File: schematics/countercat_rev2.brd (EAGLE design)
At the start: 50.8 x 50.8 mm, 30 parts, among them Q3 IRF520, Q4 IRF520, U4 ATMEGA328P_PDIP, Y1 16MHz

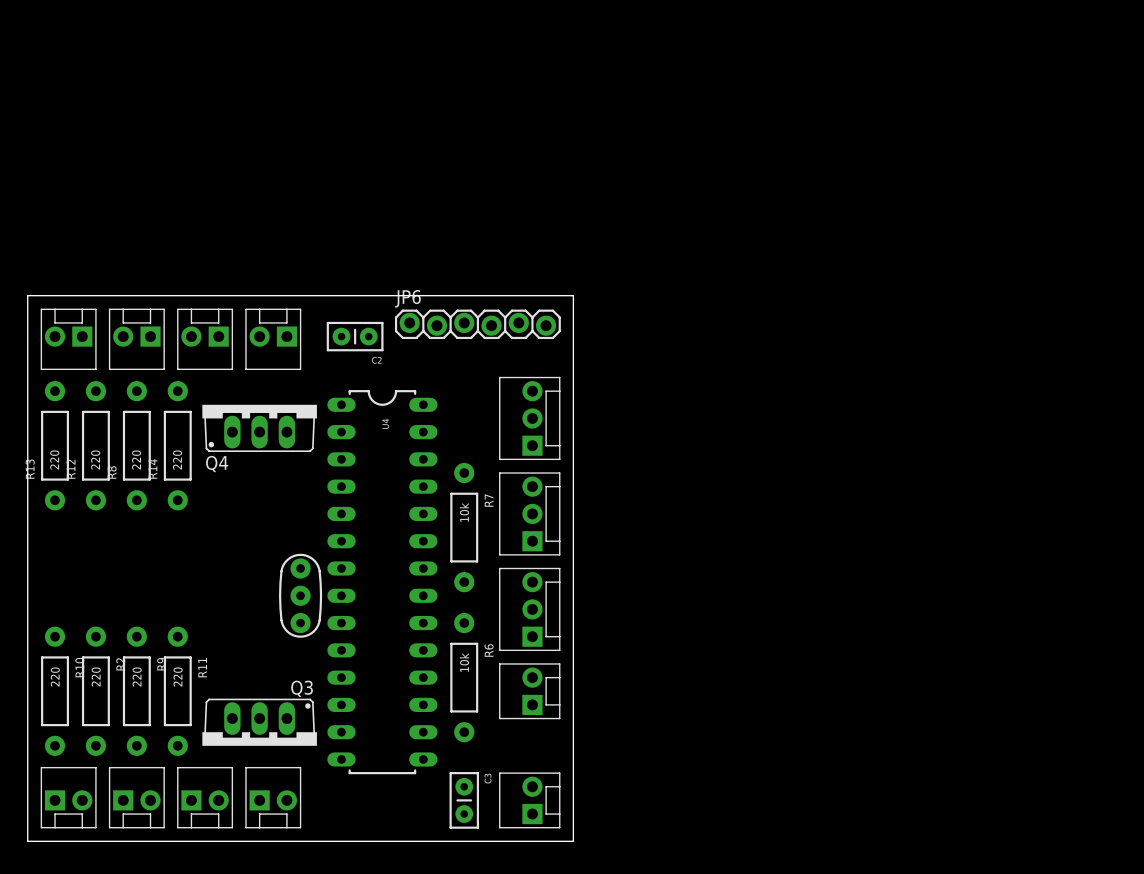
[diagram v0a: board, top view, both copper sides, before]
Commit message: Changed board size, add shifter
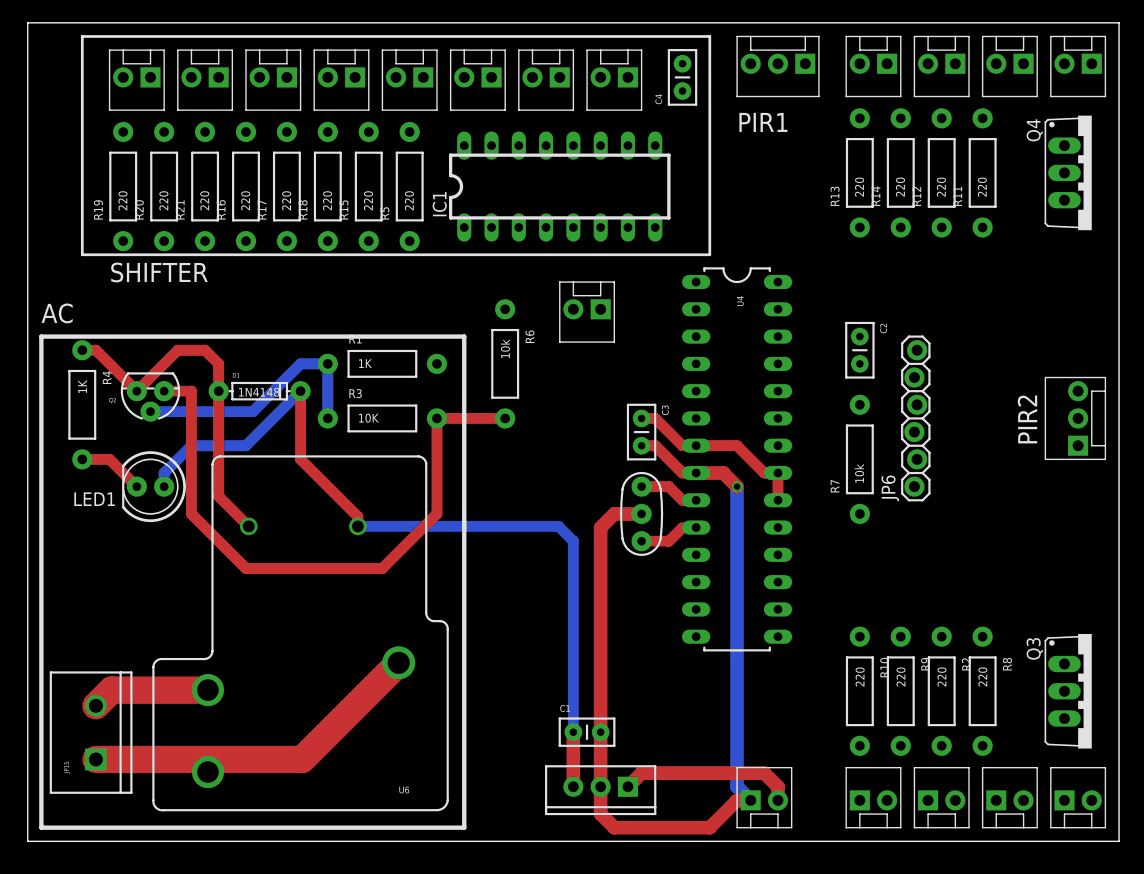
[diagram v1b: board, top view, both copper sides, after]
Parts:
- removed JP10: PWR, SparkFun:MOLEX-1X2
- added C1, C4: .1uF, SparkFun-Capacitors:CAP-PTH-SMALL2
- added D1: 1N4148, SparkFun:DIODE-1N4148
- added IC1: 74LS595N, SparkFun-DigitalIC:DIL16
- added JP15: Load, SparkFun:SCREWTERMINAL-5MM-2
- added JP16, JP17, JP18, JP19, JP20, JP21, JP22: RED1, SparkFun:MOLEX-1X2
- added JP23: PWR, SparkFun:MOLEX-1X2
- added LED1: (no value), SparkFun:LED5MM
- added LM7805: 5v, SparkFun-PowerIC:TO220-IGO
- added Q2: 2N3904, SparkFun:TO-92
- added R1, R4: 1K, SparkFun-Resistors:AXIAL-0.4
- added R15, R16, R17, R18, R19, R20, R21, R5: 220, SparkFun-Resistors:AXIAL-0.4
- added R3: 10K, SparkFun-Resistors:AXIAL-0.4
- added U6: RELAYPTH3, SparkFun:RELAY-T9A-2
- JP2: value RELAY -> RED1; device SparkFun:MOLEX-1X3 -> SparkFun:MOLEX-1X2
- moved JP11 108.3 mm to (99.1, 72.4), turned to 180 degrees
- moved R11 89.1 mm to (88.9, 62.2), turned to 90 degrees
- moved JP4 84.3 mm to (96.5, 3.81), turned to 0 degrees
- moved R12 82.7 mm to (85.1, 62.2)
- moved R8 82.0 mm to (88.9, 14.0), turned to 270 degrees
- moved JP3 81.3 mm to (90.2, 3.81)
- moved Q4 80.4 mm to (99.1, 62.2), turned to 270 degrees
- moved JP12 79.1 mm to (92.7, 72.4)
- moved JP13 79.1 mm to (80.0, 72.4)
- moved JP14 79.1 mm to (86.4, 72.4)
- moved R13 79.1 mm to (77.5, 62.2)
- moved R2 78.7 mm to (85.1, 14.0)
- moved Q3 77.6 mm to (99.1, 14.0), turned to 270 degrees
- moved JP8 74.9 mm to (77.5, 3.81)
- moved R10 74.9 mm to (77.5, 14.0)
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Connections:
- removed net FLASH: U4.15
- removed net N$12: C3.1
- removed net SPI_MISO: U4.18
- removed net SPI_MOSI: U4.17
- removed net SPI_SCK: U4.19
- new net COIL: D1.A, Q2.3, R4.P$1, U6.COIL2
- new net LOAD1: JP15.1, U6.MAIN
- new net LOAD2: JP15.2, U6.NO
- new net N$1: IC1.9
- new net N$10: JP2.1, R5.P$2
- new net N$11: JP16.1, R15.P$2
- new net N$14: JP19.1, R16.P$2
- new net N$17: JP18.1, R17.P$2
- new net N$20: JP17.1, R18.P$2
- new net N$23: JP22.1, R19.P$2
- new net N$24: JP21.1, R20.P$2
- new net N$25: JP20.1, R21.P$2
- new net N$26: IC1.15, R5.P$1
- new net N$27: IC1.1, R15.P$1
- new net N$28: IC1.2, R16.P$1
- new net N$29: IC1.3, R17.P$1
- new net N$30: IC1.4, R18.P$1
- new net N$31: IC1.5, R19.P$1
- new net N$32: IC1.6, R20.P$1
- new net N$33: IC1.7, R21.P$1
- new net N$6: Q2.2, R1.P$1, R3.P$1
- new net N$9: LED1.K, R4.P$2
- new net RCLK: IC1.12, U4.12
- new net SER: IC1.14, U4.6
- new net SRCLK: IC1.11, U4.11
- new net VB: JP23.2, LM7805.IN
- net 5V: now also C1.1, C4.2, D1.C, IC1.10, IC1.16, LED1.A, LM7805.OUT, U6.COIL1; no longer JP10.2, JP2.1
- net GND: now also C1.2, C4.1, IC1.13, IC1.8, JP16.2, JP17.2, JP18.2, JP19.2, JP20.2, JP21.2, JP22.2, JP23.1, LM7805.GND, Q2.1, R3.P$2; no longer JP10.1
- net N$8: now also C3.1
- net RELAY: now also R1.P$2; no longer JP2.3
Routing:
- net GND: track 0.00 -> 143.0 mm, vias 0 -> 1
- net 5V: track 0.00 -> 75.4 mm
- net COIL: track 0.00 -> 32.7 mm
- net LOAD1: track 0.00 -> 31.9 mm
- net N$6: track 0.00 -> 23.4 mm
- net N$8: track 0.00 -> 17.3 mm
- net VB: track 0.00 -> 16.3 mm
- net LOAD2: track 0.00 -> 11.0 mm
- net N$9: track 0.00 -> 6.13 mm
- net N$3: track 0.00 -> 5.61 mm
- net N$7: track 0.00 -> 4.34 mm
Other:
- board size 50.8 x 50.8 mm -> 101.6 x 76.2 mm
- board text added: "AC"
- board text added: "PIR1"
- board text added: "PIR2"
- board text added: "SHIFTER"

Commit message: Updated board and schematic
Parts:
- removed R10, R12, R13, R14, R15, R16, R17, R18, R19, R20, R21, R5: 220, SparkFun-Resistors:AXIAL-0.4
- added BLU, GRN, RED, YLW: (no value), SparkFun-LED:LED3MM
- added C5: .1uF, SparkFun-Capacitors:CAP-PTH-SMALL2
- added JP10: RED_RAW, SparkFun:MOLEX-1X2
- added JP24: GRN_RAW, SparkFun:MOLEX-1X2
- added JP25: BLU1, SparkFun:MOLEX-1X2
- added JP26: BLU2, SparkFun:MOLEX-1X2
- added JP27: BLU3, SparkFun:MOLEX-1X2
- added JP28: BLU4, SparkFun:MOLEX-1X2
- added JP29: BLU_RAW, SparkFun:MOLEX-1X2
- added JP30: YLW1, SparkFun:MOLEX-1X2
- added JP31: YLW2, SparkFun:MOLEX-1X2
- added JP32: YLW3, SparkFun:MOLEX-1X2
- added JP33: YLW4, SparkFun:MOLEX-1X2
- added JP34: YLW_RAW, SparkFun:MOLEX-1X2
- added JP35: AUX, SparkFun-Connectors:1X08_LOCK
- added JP36: AUX_PWR, SparkFun:MOLEX-1X2
- added Q1, Q5: IRF520, transistor-power:TO220BV
- added R35: R-GRN, SparkFun-Resistors:RPACK-SIP-PTH-5
- JP16: value RED1 -> SHF3
- JP17: value RED1 -> SHF5
- JP18: value RED1 -> SHF1
- JP19: value RED1 -> SHF2
- JP2: value RED1 -> SHF4
- JP20: value RED1 -> SHF8
- JP21: value RED1 -> SHF7
- JP22: value RED1 -> SHF6
- R11: value 220 -> R-SHF; device SparkFun-Resistors:AXIAL-0.4 -> SparkFun-Resistors:RPACK-SIP-PTH-8
- R2: value 220 -> R-RED; device SparkFun-Resistors:AXIAL-0.4 -> SparkFun-Resistors:RPACK-SIP-PTH-5
- R8: value 220 -> R-BLU; device SparkFun-Resistors:AXIAL-0.4 -> SparkFun-Resistors:RPACK-SIP-PTH-5
- R9: value 220 -> R-YLW; device SparkFun-Resistors:AXIAL-0.4 -> SparkFun-Resistors:RPACK-SIP-PTH-5
- moved R11 57.8 mm to (31.1, 64.1), turned to 270 degrees
- moved JP3 51.6 mm to (99.1, 54.6), turned to 180 degrees
- moved JP4 50.9 mm to (92.7, 54.6), turned to 180 degrees
- moved JP7 50.9 mm to (86.4, 54.6), turned to 180 degrees
- moved JP8 50.9 mm to (80.0, 54.6), turned to 180 degrees
- moved JP9 47.3 mm to (62.9, 3.17), turned to 0 degrees
- moved R6 35.2 mm to (61.0, 13.3), turned to 0 degrees
- moved R2 34.5 mm to (88.9, 48.3)
- moved Q3 31.9 mm to (69.8, 26.7), turned to 90 degrees
- moved Q4 30.2 mm to (69.8, 69.8), turned to 90 degrees
- moved C4 28.7 mm to (33.7, 61.0), turned to 270 degrees
- moved JP18 19.7 mm to (56.5, 71.1)
- moved JP19 19.7 mm to (50.2, 71.1)
- moved JP2 18.4 mm to (37.5, 71.1)
- moved R9 13.4 mm to (88.3, 2.54)
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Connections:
- removed net N$22 (its old number): JP8.2, R10.P$2
- removed net SFW_RXI: U4.4
- removed net SFW_TXO: U4.5
- new net B0: JP35.3, U4.14
- new net B1: JP35.4, U4.15
- new net BLU: Q3.G, U4.4
- new net D7: JP35.2, U4.13
- new net N$12: JP4.2, R2.P$3
- new net N$18: JP7.2, R2.P$4
- new net N$34: BLU.K, JP25.1, JP26.1, JP27.1, JP28.1, JP29.1, Q3.D
- new net N$35: JP26.2, R8.P$3
- new net N$36: JP27.2, R8.P$4
- new net N$37: JP28.2, R8.P$5
- new net N$38: BLU.A, R8.P$6
- new net N$39: JP25.2, R8.P$2
- new net N$40: JP30.1, JP31.1, JP32.1, JP33.1, JP34.1, Q5.D, YLW.K
- new net N$41: JP31.2, R9.P$3
- new net N$42: JP32.2, R9.P$4
- new net N$43: JP33.2, R9.P$5
- new net N$44: R9.P$6, YLW.A
- new net N$45: GRN.A, R35.P$6
- new net N$46: JP30.2, R9.P$2
- new net SPI_MISO: JP35.7, U4.18
- new net SPI_MOSI: JP35.6, U4.17
- new net SPI_SCK: JP35.8, U4.19
- new net YLW: Q5.G, U4.5
- net 5V: now also JP10.2, JP24.2, JP29.2, JP34.2, JP36.1, R35.P$1; no longer JP6.4, R10.P$1, R11.P$1, R12.P$1, R13.P$1, R14.P$1
- net GND: now also C5.2, JP35.1, JP36.2, Q1.S, Q5.S, R11.P$1; no longer JP16.2, JP17.2, JP18.2, JP19.2, JP2.2, JP20.2, JP21.2, JP22.2
- net N$1: now also IC1.4, JP17.1; no longer IC1.9
- net N$10: now also JP18.2, R11.P$2; no longer JP2.1, R5.P$2
- net N$11: now also JP19.2, R11.P$3; no longer JP16.1, R15.P$2
- net N$13: now also R35.P$3; no longer R12.P$2
- net N$14: now also JP16.2, R11.P$4; no longer JP19.1, R16.P$2
- net N$15: now also R35.P$4; no longer R13.P$2
- net N$16: now also R35.P$5; no longer R14.P$2
- net N$17: now also JP2.2, R11.P$5; no longer JP18.1, R17.P$2
- net N$19: now also JP8.2, R2.P$5; no longer JP4.2, R8.P$2
- net N$2: now also JP10.1, Q1.D, RED.K; no longer Q3.D
- net N$20: now also JP17.2, R11.P$6; no longer JP17.1, R18.P$2
- net N$21: now also R2.P$6, RED.A; no longer JP7.2, R9.P$2
- net N$23: now also JP22.2, R11.P$7; no longer JP22.1, R19.P$2
- net N$24: now also JP21.2, R11.P$8; no longer JP21.1, R20.P$2
- net N$25: now also JP20.2, R11.P$9; no longer JP20.1, R21.P$2
- net N$26: now also JP18.1; no longer R5.P$1
- net N$27: now also JP19.1; no longer R15.P$1
- net N$28: now also JP16.1; no longer R16.P$1
- net N$29: now also JP2.1; no longer R17.P$1
- net N$30: now also IC1.6, JP21.1; no longer IC1.4, R18.P$1
- net N$31: now also JP22.1; no longer R19.P$1
- net N$32: now also IC1.7, JP20.1; no longer IC1.6, R20.P$1
- net N$33: now also JP6.4; no longer IC1.7, R21.P$1
- net N$4: now also GRN.K, JP24.1, Q4.D
- net N$5: now also R35.P$2; no longer R11.P$2
- net RED: now also Q1.G; no longer Q3.G
- net SPI_CS: now also JP35.5
- net VB: now also C5.1
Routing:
- net GND: track 143.0 -> 46.2 mm, vias 1 -> 0
- net 5V: track 75.4 -> 142.7 mm
- net N$40: track 0.00 -> 54.5 mm
- net N$2: track 0.00 -> 50.5 mm
- net N$4: track 0.00 -> 46.0 mm
- net N$21: track 0.00 -> 44.3 mm
- net N$34: track 0.00 -> 42.9 mm
- net N$44: track 0.00 -> 41.5 mm
- net COIL: track 32.7 -> 0.00 mm
- net N$6: track 23.4 -> 0.00 mm
- net N$8: track 17.3 -> 0.00 mm
- net N$45: track 0.00 -> 16.6 mm
- net N$5: track 0.00 -> 14.6 mm
- net PUSH: track 0.00 -> 14.2 mm
- net N$46: track 0.00 -> 13.2 mm
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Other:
- board text added: "+"
- board text added: "+5V"
- board text added: "< 10A"
- board text added: "AC RELAY"
- board text added: "B0"
- board text added: "B1"
- board text added: "Blue"
- board text added: "CS"
- board text added: "CounterCat"
- board text added: "D7"
- board text added: "DTR"
- board text added: "GND"
- board text added: "GRN"
- board text added: "MISO"
- board text added: "MOSI"
- board text added: "PUSH"
- board text added: "RED"
- board text added: "SCLK"
- board text added: "Ylw"
- board text removed: "AC"

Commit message: Autorouted and adjusted results
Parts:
- moved RED 1.27 mm to (93.3, 61.6)
- moved JP10 0.64 mm to (85.7, 62.2)
- moved R4 0.64 mm to (1.91, 40.6)
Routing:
- net GND: track 46.2 -> 288.9 mm
- net 5V: track 142.7 -> 298.5 mm
- net SPI_CS: track 0.00 -> 99.6 mm, vias 0 -> 1
- net SPI_MOSI: track 0.00 -> 94.0 mm, vias 0 -> 1
- net B1: track 0.00 -> 93.4 mm, vias 0 -> 1
- net SPI_MISO: track 0.00 -> 81.6 mm, vias 0 -> 1
- net D7: track 0.00 -> 78.8 mm, vias 0 -> 1
- net SPI_SCK: track 0.00 -> 78.0 mm, vias 0 -> 1
- net B0: track 0.00 -> 76.3 mm, vias 0 -> 1
- net BLU: track 0.00 -> 57.8 mm
- net N$11: track 0.00 -> 52.9 mm
- net DTR: track 0.00 -> 50.1 mm
- net N$32: track 0.00 -> 49.9 mm
- net YLW: track 0.00 -> 49.1 mm
- net SRCLK: track 0.00 -> 47.6 mm
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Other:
- board text added: "-"
- board text added: "16MHz"
- board text added: "Andrew Kessler 1/14"
- board text added: "CounterCat Rev3"
- board text added: "Grn"
- board text added: "Raw"
- board text added: "Red"
- board text removed: "CounterCat"
- board text removed: "GRN"
- board text removed: "RED"

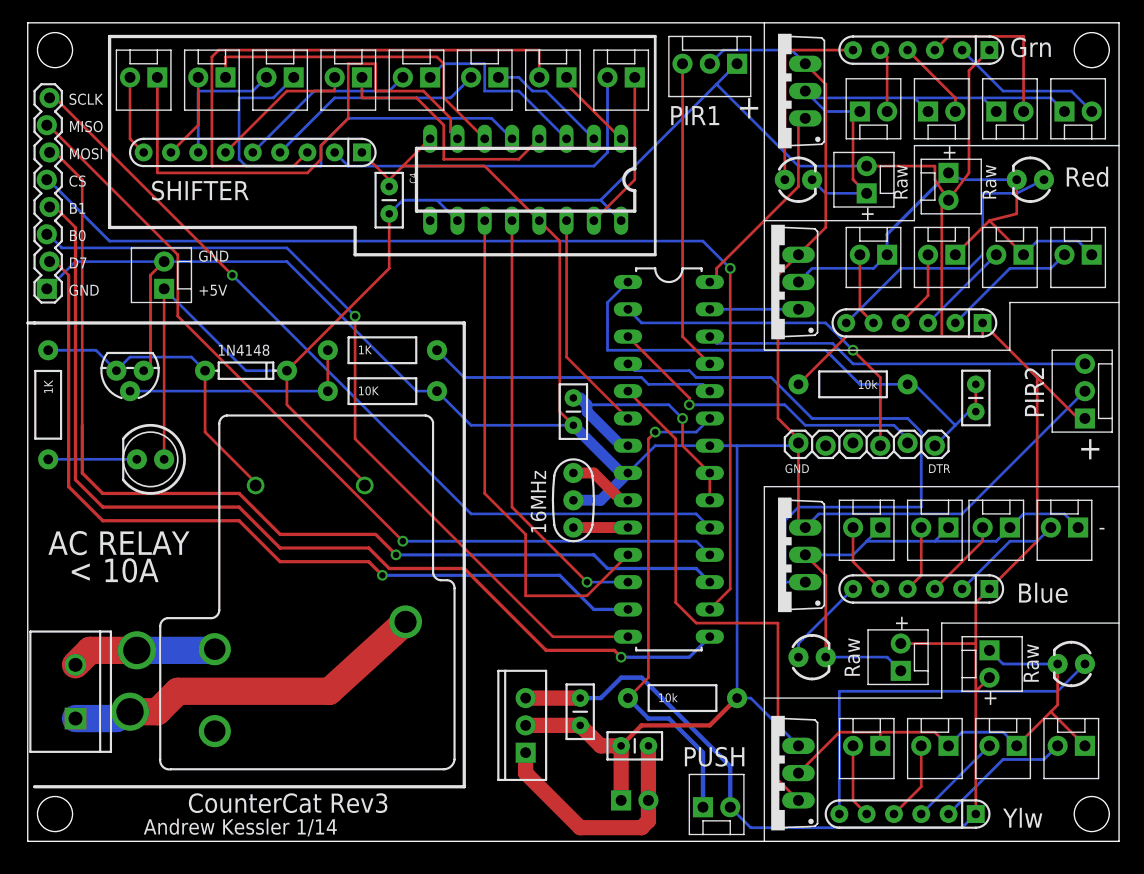
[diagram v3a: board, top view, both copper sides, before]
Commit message: Autorouted and DRC'd
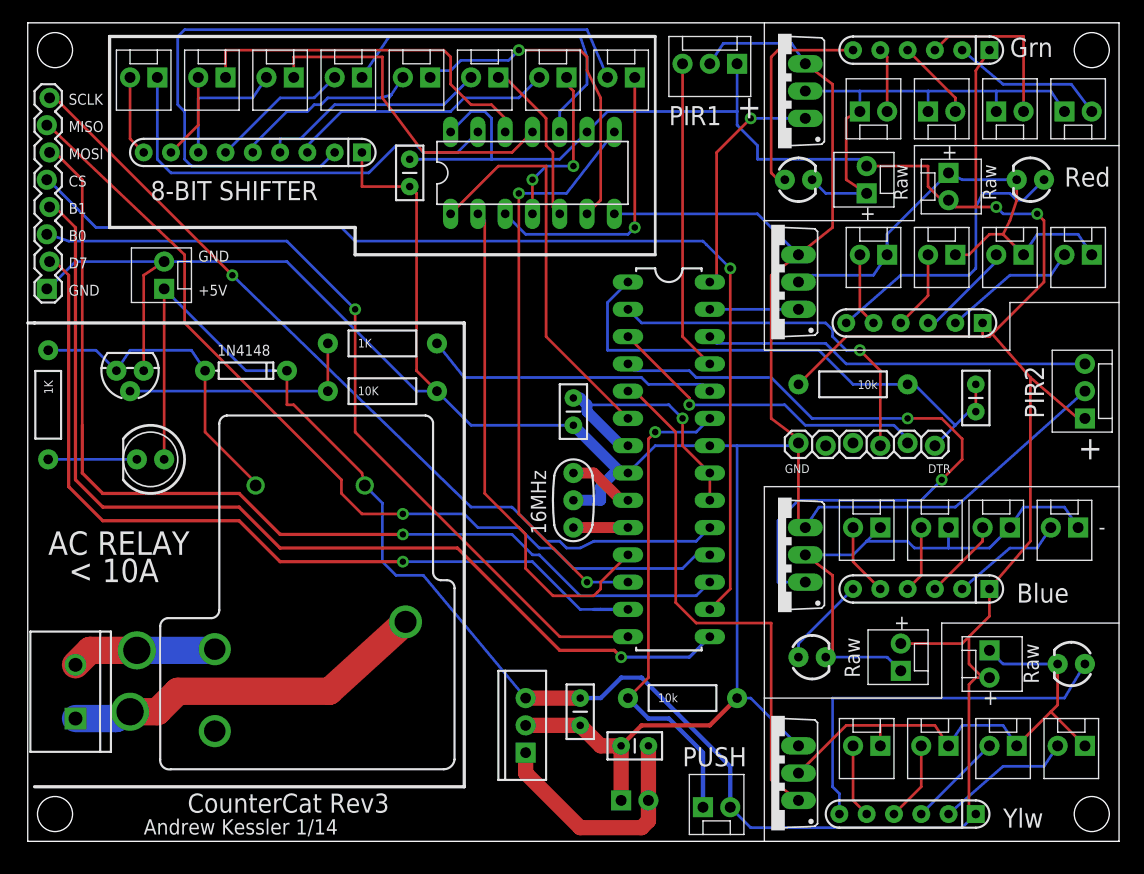
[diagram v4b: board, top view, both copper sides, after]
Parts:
- removed C4: .1uF, SparkFun-Capacitors:CAP-PTH-SMALL2
- removed IC1: 74LS595N, SparkFun-DigitalIC:DIL16
- added C6: .1uF, SparkFun-Capacitors:CAP-PTH-SMALL2
- added U$15: 74XX164, andrews_eagle_lib:DIP14
- moved R1 0.63 mm to (33.0, 46.4)
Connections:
- removed net RCLK: IC1.12, U4.12
- removed net SER: IC1.14, U4.6
- new net DSA: U$15.1, U4.6
- new net DSB: U$15.2, U4.11
- net 5V: now also C6.2, U$15.14, U$15.9; no longer C4.2, IC1.10, IC1.16
- net GND: now also C6.1, U$15.7; no longer C4.1, IC1.13, IC1.8
- net N$1: now also U$15.10; no longer IC1.4
- net N$26: now also U$15.3; no longer IC1.15
- net N$27: now also U$15.4; no longer IC1.1
- net N$28: now also U$15.5; no longer IC1.2
- net N$29: now also U$15.6; no longer IC1.3
- net N$30: now also U$15.12; no longer IC1.6
- net N$31: now also U$15.11; no longer IC1.5
- net N$32: now also U$15.13; no longer IC1.7
- net SRCLK: now also U$15.8, U4.12; no longer IC1.11, U4.11
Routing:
- net DSB: track 0.00 -> 47.4 mm
- net RCLK: track 40.4 -> 0.00 mm, vias 1 -> 0
- net DSA: track 0.00 -> 37.4 mm
- net N$10: track 33.4 -> 69.7 mm
- net N$11: track 52.9 -> 24.9 mm
- net SER: track 20.8 -> 0.00 mm
- net 5V: track 298.5 -> 317.9 mm, vias 0 -> 2
- net N$29: track 17.6 -> 31.4 mm, vias 0 -> 1
- net N$26: track 14.9 -> 27.1 mm, vias 0 -> 1
- net N$32: track 49.9 -> 40.1 mm
- net N$31: track 41.0 -> 31.3 mm
- net N$1: track 23.4 -> 32.4 mm
- net N$27: track 7.82 -> 16.0 mm, vias 0 -> 2
- net SRCLK: track 47.6 -> 54.3 mm, vias 0 -> 2
- net BLU: track 57.8 -> 63.7 mm, vias 0 -> 2
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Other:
- board text added: "8-BIT SHIFTER"
- board text removed: "SHIFTER"
